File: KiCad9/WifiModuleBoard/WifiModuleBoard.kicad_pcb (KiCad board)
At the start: 2 copper layers, 27.6 x 20.4 mm, 10 parts, among them J2 Conn_01x07_Pin, J3 TC2030, J4 Conn_01x05_Pin, U1 ESP32-C5-WROOM-1U-N8R8

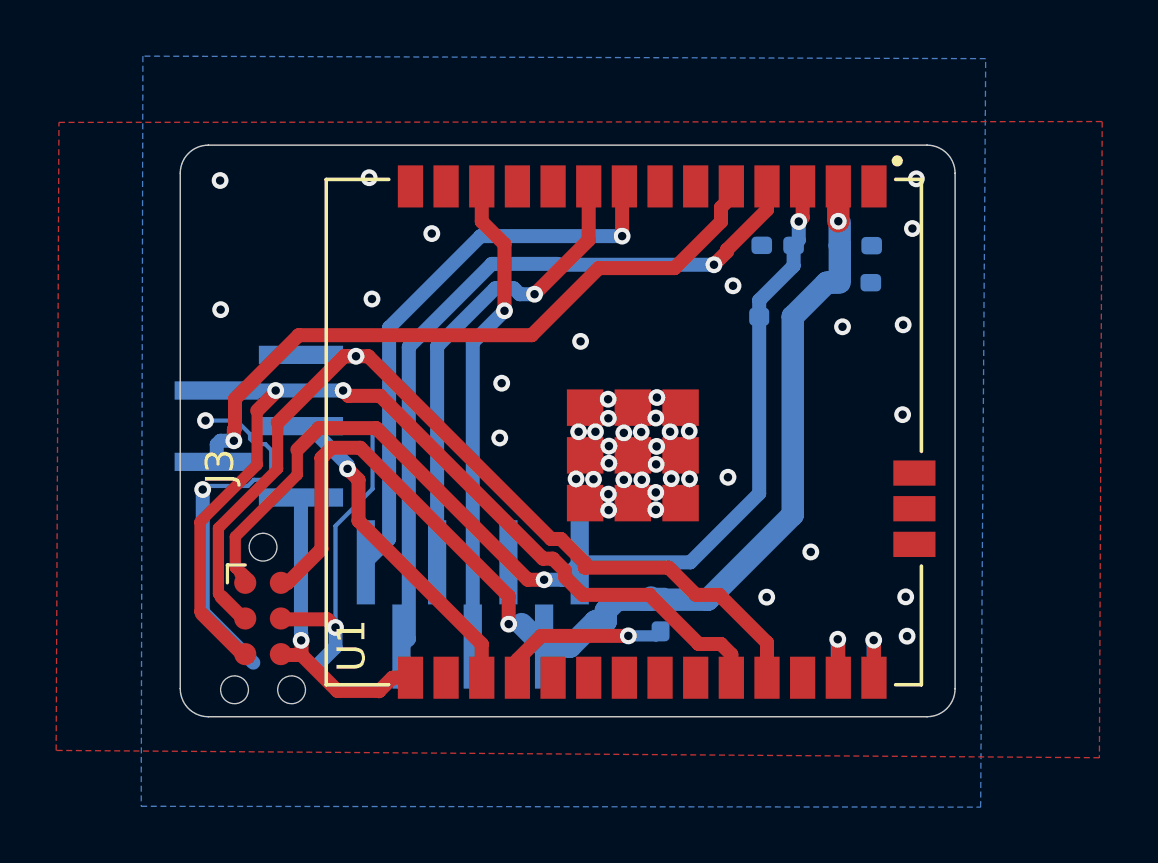
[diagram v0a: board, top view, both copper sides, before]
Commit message: add 3d of wifiboard
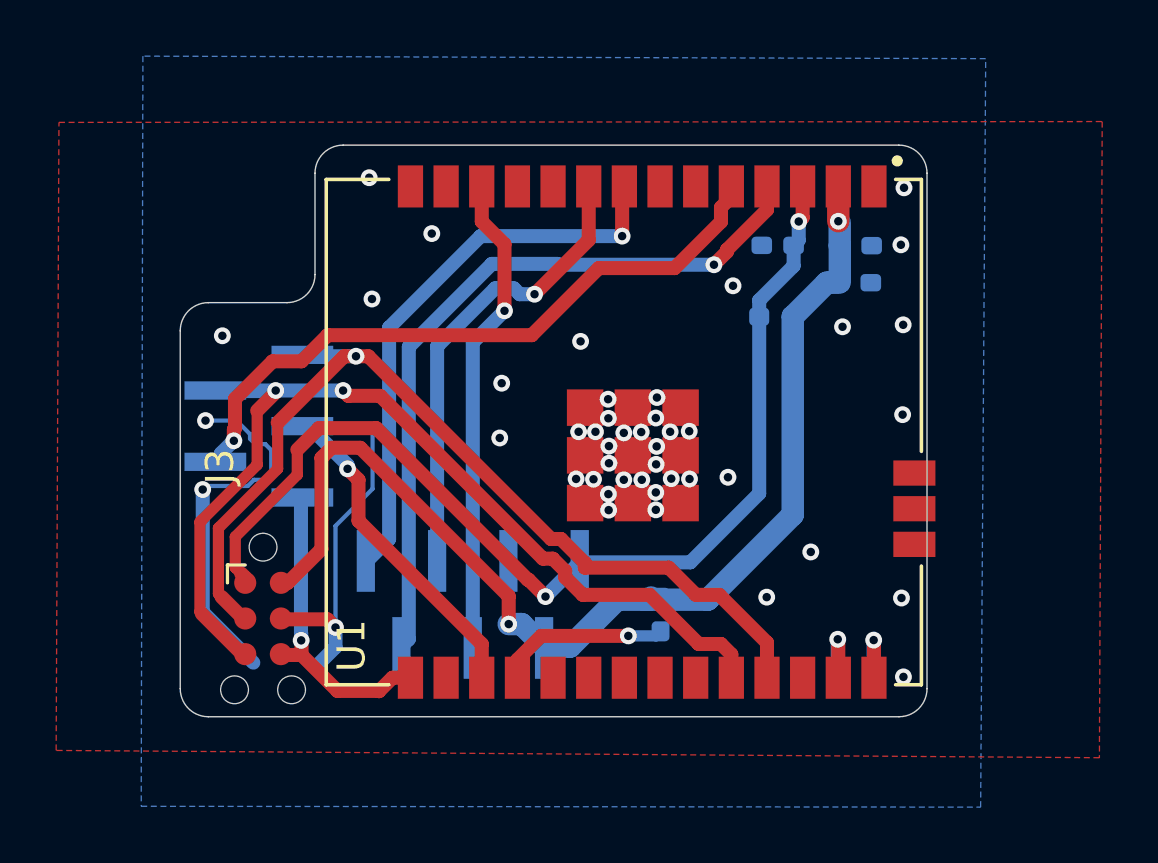
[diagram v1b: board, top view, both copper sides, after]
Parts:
- C1: value 0.1uF -> 10uF
- C2: value 22uF -> 10uF
- C3: value 0.1uF -> 100nF
- J2: footprint Connector_PinHeader_1.27mm:PinHeader_1x07_P1.27mm_Vertical_SMD_Pin1Left -> WiRoc:PinSocket_1x07_P1.27mm_Vertical_SMD_Pin1Left_ForMaleOrFemale
- J4: footprint Connector_PinHeader_1.27mm:PinHeader_1x05_P1.27mm_Vertical_SMD_Pin1Left -> WiRoc:PinSocket_1x05_P1.27mm_Vertical_SMD_Pin1Left_MaleOrFemale
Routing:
- net GND: vias 47 -> 46
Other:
- board size 27.6 x 20.4 mm -> 26.6 x 20.4 mm

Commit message: etc
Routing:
- net GND: track 27.0 -> 8.25 mm, vias 46 -> 58
- net VDD_SYS_3.3V: track 40.5 -> 34.3 mm
- net /WIFI-DataReady: track 12.1 -> 17.5 mm
- net TX0: track 34.3 -> 37.2 mm
- net RX0: track 36.5 -> 38.2 mm
- net /Enable: track 38.2 -> 36.6 mm
